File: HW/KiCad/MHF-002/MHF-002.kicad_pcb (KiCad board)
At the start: 2 copper layers, 228 x 101.2 mm, 289 parts, among them J1 VGA, J10 I2C, J100 x, J101 x, J102 x, J103 x, J104 x, J105 x, J106 x, J107 +3V3, J108 GND, J109 +3V3, J11 + 5V -, J110 +5V, J111 GND, J112 GND, J113 SDCard, J12 Reset, J13 +5V, J14 GND, J15 AREF, J16 XTAL2, J17 SDcard, J18 XTAL1, J19 AVCC, J2 PS/2, J20 SDcardpins, J21 x, J22 x, J23 VIN 12V, J24 AND_B1, J25 AND_B2, J26 AND_C1, J27 AND_C2, J28 AND_D1, J29 AND_D2, J3 RCA, J30 AND_Dx, J31 AND_Cx, J32 AND_Bx, J33 NOTF, J34 NOTE, J35 NOTEx, J36 NOTFx, J37 x, J38 x, J39 x, J4 SysBus, J40 x, J41 x, J42 x, J43 x, J44 x, J45 x, J46 x, J47 x, J48 x, J49 x, J5 Micro, J50 x, J51 x, J52 x, J53 x, J54 x, J55 x, J56 x, J57 x, J58 x, J59 x, J6 SysBus, J60 x, J61 x, J62 x, J63 x, J64 x, J65 x, J66 x, J67 x, J68 x, J69 x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

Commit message: footprints (maybe complete)
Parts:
- C1: footprint Capacitor_THT:C_Disc_D4.3mm_W1.9mm_P5.00mm -> MHF:C_Disc_D4.3mm_W1.9mm_P5.00mm
- C10, C11, C13, C14, C15, C16, C2, C5, C6, C7, C8: footprint Capacitor_SMD:C_0603_1608Metric_Pad1.08x0.95mm_HandSolder -> MHF:C_0805_2012Metric_HandSolder
- C12, C9, Cx1, Cx10, Cx11, Cx12, Cx13, Cx2, Cx3, Cx4, Cx5, Cx6, Cx7, Cx8, Cx9: footprint Capacitor_THT:C_Disc_D3.0mm_W2.0mm_P2.50mm -> MHF:C_Disc_D3.0mm_W2.0mm_P2.50mm
- C3, C4: value 100n -> 22n; footprint Capacitor_SMD:C_0603_1608Metric_Pad1.08x0.95mm_HandSolder -> MHF:C_0805_2012Metric_HandSolder
- Cx14, Cx15: footprint Capacitor_THT:CP_Radial_D5.0mm_P2.50mm -> MHF:CP_Radial_D5.0mm_P2.50mm
- D1: footprint Diode_THT:D_DO-41_SOD81_P10.16mm_Horizontal -> MHF:D_DO-41_SOD81_P10.16mm_Horizontal
- D2: footprint Diode_SMD:D_1206_3216Metric -> MHF:D_1210_3225Metric_HandSolder
- D3: footprint Diode_SMD:D_1210_3225Metric -> MHF:D_1210_3225Metric_HandSolder
- F1: footprint Fuse:Fuse_1206_3216Metric_Pad1.42x1.75mm_HandSolder -> MHF:Fuse_1206_3216Metric_Pad1.42x1.75mm_HandSolder
- H5, H6, H7, H8: footprint MountingHole:MountingHole_3.2mm_M3_Pad -> MHF:MountingHole_3.2mm_M3_Pad
- J1: footprint Connector_Dsub:DSUB-15-HD_Socket_Horizontal_P2.29x2.54mm_EdgePinOffset8.35mm_Housed_MountingHolesOffset10.89mm -> MHF:DSUB-15-HD_Socket_Horizontal_P2.29x2.54mm_EdgePinOffset8.35mm_Housed_MountingHolesOffset10.89mm
- J10, J20: footprint Connector_PinHeader_2.54mm:PinHeader_1x04_P2.54mm_Vertical -> MHF:PinHeader_1x04_P2.54mm_Vertical
- J100, J101, J102, J103, J104, J105, J106, J107, J108, J109, J110, J111, J112, J12, J13, J14, J15, J16, J18, J19, J21, J22, J24, J25, J26, J27, J28, J29, J30, J31, J32, J33, J34, J35, J36, J37, J38, J39, J40, J41, J42, J43, J44, J45, J46, J47, J48, J49, J50, J51, J52, J53, J54, J55, J56, J57, J58, J59, J60, J61, J62, J63, J64, J65, J66, J67, J68, J69, J70, J71, J72, J73, J74, J75, J76, J77, J78, J79, J80, J81, J82, J83, J84, J85, J86, J87, J88, J89, J90, J91, J92, J93, J94, J95, J96, J97, J98, J99: footprint Gilhad:PinHole_1x01_2.54xrectangle -> MHF:PinHole_1x01_2.54xrectangle
- J11: footprint Connector_PinSocket_2.54mm:PinSocket_2x03_P2.54mm_Vertical -> MHF:PinSocket_2x03_P2.54mm_Vertical
- J17, J7, J9, JP27, PG1: footprint Connector_PinHeader_2.54mm:PinHeader_1x06_P2.54mm_Vertical -> MHF:PinHeader_1x06_P2.54mm_Vertical
- J23: footprint Connector_BarrelJack:BarrelJack_Horizontal -> MHF:BarrelJack_Horizontal
- J4: footprint Connector_PinSocket_2.54mm:PinSocket_2x32_P2.54mm_Vertical -> MHF:PinSocket_2x32_P2.54mm_Vertical
- J5: footprint Connector_USB:USB_Micro-B_XKB_U254-051T-4BH83-F1S -> MHF:USB_Micro-B_XKB_U254-051T-4BH83-F1S
- J6: footprint Connector_PinHeader_2.54mm:PinHeader_2x32_P2.54mm_Vertical -> MHF:PinHeader_2x32_P2.54mm_Vertical
- J8: footprint Connector_PinHeader_2.54mm:PinHeader_2x03_P2.54mm_Vertical -> MHF:PinHeader_2x03_P2.54mm_Vertical
- JP1, JP10, JP11, JP12, JP13, JP14, JP2, JP3, JP4, JP5, JP6, JP7, JP8, JP9, JP91: footprint Jumper:SolderJumper-2_P1.3mm_Bridged_Pad1.0x1.5mm -> MHF:SolderJumper-2_P1.3mm_Bridged_Pad1.0x1.5mm
- JP100, JP102, JP103, JP104, JP105, JP106, JP107, JP92, JP94, JP95, JP98, JP99: footprint Jumper:SolderJumper-3_P1.3mm_Open_RoundedPad1.0x1.5mm -> MHF:SolderJumper-3_P1.3mm_Open_RoundedPad1.0x1.5mm
- JP15, JP16, JP17, JP18, JP19, JP21, JP22, JP23, JP24, JP25, JP55, JP56: footprint Jumper:SolderJumper-2_P1.3mm_Open_RoundedPad1.0x1.5mm -> MHF:SolderJumper-2_P1.3mm_Open_RoundedPad1.0x1.5mm
- JP26, JP28: footprint Connector_PinHeader_2.54mm:PinHeader_1x02_P2.54mm_Vertical -> MHF:PinHeader_1x02_P2.54mm_Vertical
- LED1, LED10, LED2, LED3, LED4, LED5, LED6, LED7, LED8, LED9: footprint LED_SMD:LED_0805_2012Metric -> MHF:LED_0805_2012Metric
- N1, N3: footprint NetTie:NetTie-2_SMD_Pad0.5mm -> MHF:NetTie-2_SMD_Pad0.5mm
- PA1, PB1, PC1, PD1, PE1, PF1, PH1, PJ1, PK1, PL1: footprint Connector_PinHeader_2.54mm:PinHeader_1x08_P2.54mm_Vertical -> MHF:PinHeader_1x08_P2.54mm_Vertical
- Q1: footprint Package_TO_SOT_THT:TO-92_Inline -> MHF:TO-92_Inline
- R1, R10, R11, R12, R13, R14, R15, R16, R17, R18, R19, R2, R20, R21, R22, R23, R3, R32, R33, R38, R39, R4, R41, R43, R44, R45, R46, R47, R5, R6, R7, R8, R9: footprint Resistor_SMD:R_0805_2012Metric_Pad1.20x1.40mm_HandSolder -> MHF:R_0805_2012Metric_Pad1.20x1.40mm_HandSolder
- R24, R25, R26, R27, R28, R29, R30, R31, R34, R35, R36, R37, R40, R42: footprint Resistor_SMD:R_0603_1608Metric_Pad0.98x0.95mm_HandSolder -> MHF:R_0805_2012Metric_Pad1.20x1.40mm_HandSolder
- U13: footprint Package_SO:SOIC-16_3.9x9.9mm_P1.27mm -> MHF:SOIC-16_3.9x9.9mm_P1.27mm
- U14, U15: footprint Package_TO_SOT_SMD:SOT-223-3_TabPin2 -> MHF:SOT-223-3_TabPin2_HandSolder
- U2, U3: footprint Package_DIP:DIP-14_W7.62mm -> MHF:SOIC-14_3.9x8.7mm_P1.27mm
- U4: footprint Package_SO:TSSOP-20_4.4x5mm_P0.5mm -> MHF:TSSOP-20_4.4x6.5mm_P0.65mm_HandSolder; moved to B.Cu
- U5: footprint MHF:G_SOIC-16_3.9x9.9mm_HandSolder -> MHF:SOIC-16_3.9x9.9mm_P1.27mm
- U7, U8, U9: footprint Package_DIP:DIP-16_W7.62mm -> MHF:SOIC-16_3.9x9.9mm_P1.27mm
- Y1, Y2: footprint Crystal:Crystal_SMD_HC49-SD -> MHF:Crystal_SMD_HC49-SD
- moved C8 220.5 mm to (306.1, 47.8)
- moved C7 220.5 mm to (301.6, 44.9)
- moved C5 220.5 mm to (311.7, 41.4)
- moved C6 220.5 mm to (309.4, 38.7)
- moved U7 189.4 mm to (247.9, -6.94)
- moved J5 175.1 mm to (251.9, -19.9)
- moved Q1 165.7 mm to (252.1, -39.4)
- moved JP20 160.3 mm to (268.5, 136.9)
- moved JP30 160.3 mm to (268.5, 144.5)
- moved JP31 160.3 mm to (268.5, 139.4)
- moved JP32 160.3 mm to (268.5, 141.9)
- moved F1 143.7 mm to (261.1, 35.7)
- moved D3 139.2 mm to (187.1, 141.3)
- moved U15 138.7 mm to (200.9, 156.2)
- moved J17 123.6 mm to (182.9, 82.5)
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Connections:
- M3 pad 13: /L7 -> /L4
- M3 pad 14: /L6 -> /L5
- M3 pad 15: /L5 -> /L6
- M3 pad 16: /L4 -> /L7
- M3 pad 17: /L0 -> /L3
- M3 pad 18: /L1 -> /L2
- M3 pad 19: /L2 -> /L1
- M3 pad 20: /L3 -> /L0
- U4 pad 16: /L0 -> /L3
- U4 pad 17: /L1 -> /L2
- U4 pad 18: /L2 -> /L1
- U4 pad 19: /L3 -> /L0
- U4 pad 2: XAD3 -> XAD7
- U4 pad 3: XAD2 -> XAD6
- U4 pad 4: XAD1 -> XAD5
- U4 pad 5: XAD0 -> XAD4
- U4 pad 6: XAD4 -> XAD3
- U4 pad 7: XAD5 -> XAD2
- U4 pad 8: XAD6 -> XAD1
- U4 pad 9: XAD7 -> XAD0

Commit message: included all planned improvements
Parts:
- added D10: WS2812B, MHF:LED_WS2812B_PLCC4_5.0x5.0mm_P3.2mm_HandSolder, F.Cu at (353.1, 134.6)
- added D11: WS2812B, MHF:LED_WS2812B_PLCC4_5.0x5.0mm_P3.2mm_HandSolder, F.Cu at (363.2, 134.6)
- added D4: WS2812B, MHF:LED_WS2812B_PLCC4_5.0x5.0mm_P3.2mm_HandSolder, F.Cu at (289.6, 134.6)
- added D5: WS2812B, MHF:LED_WS2812B_PLCC4_5.0x5.0mm_P3.2mm_HandSolder, F.Cu at (302.3, 134.6)
- added D6: WS2812B, MHF:LED_WS2812B_PLCC4_5.0x5.0mm_P3.2mm_HandSolder, F.Cu at (312.4, 134.6)
- added D7: WS2812B, MHF:LED_WS2812B_PLCC4_5.0x5.0mm_P3.2mm_HandSolder, F.Cu at (322.6, 134.6)
- added D8: WS2812B, MHF:LED_WS2812B_PLCC4_5.0x5.0mm_P3.2mm_HandSolder, F.Cu at (332.7, 134.6)
- added D9: WS2812B, MHF:LED_WS2812B_PLCC4_5.0x5.0mm_P3.2mm_HandSolder, F.Cu at (342.9, 134.6)
- added J114: VIN, MHF:PinHole_1x01_2.54xrectangle, F.Cu at (325.2, 86.4)
- added J115: VI, MHF:PinHole_1x01_2.54xrectangle, F.Cu at (330.3, 91.4)
- added J116: GND, MHF:PinHole_1x01_2.54xrectangle, F.Cu at (325.2, 94.0)
- added JP29: SBC_D_Dir, MHF:SolderJumper-2_P1.3mm_Open_RoundedPad1.0x1.5mm, F.Cu at (337.9, 66.0)
- added JP33: SBC_A_DIR, MHF:SolderJumper-2_P1.3mm_Open_RoundedPad1.0x1.5mm, F.Cu at (330.3, 68.6)
- added JP34: SBC_G_Enable, MHF:SolderJumper-2_P1.3mm_Open_RoundedPad1.0x1.5mm, F.Cu at (337.9, 73.9)
- added JP35: SBC_S_Enable, MHF:SolderJumper-2_P1.3mm_Open_RoundedPad1.0x1.5mm, F.Cu at (330.3, 76.2)
- added JP36: SBC_Read, MHF:SolderJumper-2_P1.3mm_Open_RoundedPad1.0x1.5mm, F.Cu at (335.4, 81.3)
- added JP37: SBC_Write, MHF:SolderJumper-2_P1.3mm_Open_RoundedPad1.0x1.5mm, F.Cu at (330.3, 83.8)
- added R48: 1k, MHF:R_0805_2012Metric_Pad1.20x1.40mm_HandSolder, F.Cu at (330.3, 96.5)
- added R49: 1k, MHF:R_0805_2012Metric_Pad1.20x1.40mm_HandSolder, F.Cu at (330.3, 99.1)
- J9, PG1: footprint MHF:PinHeader_1x06_P2.54mm_Vertical -> MHF:PinHeader_1x07_P2.54mm_Vertical
- JP92: value X16 -> X_S16
- PA1, PB1, PC1, PD1, PE1, PF1, PH1, PJ1, PK1, PL1: footprint MHF:PinHeader_1x08_P2.54mm_Vertical -> MHF:PinHeader_1x09_P2.54mm_Vertical
- moved LED6 5.68 mm to (45.4, 118.4)
- moved R39 5.68 mm to (48.6, 120.4)
- moved JP20 2.86 mm to (266.7, 134.6)
- moved JP31 2.86 mm to (266.7, 137.2)
- moved JP32 2.86 mm to (266.7, 139.7)
- moved JP30 2.86 mm to (266.7, 142.2)
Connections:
- net Net-(PG1-Pin_6) renamed X_SHARE_FUTURE
- net X16 renamed X_S16
- J9 pad 5: GND -> DTR
- J9 pad 6: +5V -> GND
- JP55 pad 1: SCK -> MISO
- PD1 pad 5: X_SHARE_GRANTED -> Net-(PD1-Pin_5)
- PD1 pad 6: X_SHARE_REQUEST -> Net-(PD1-Pin_6)
- PG1 pad 5: Net-(PG1-Pin_5) -> X_SHARE_REQUEST
- U1 pad 29: Net-(PG1-Pin_5) -> X_SHARE_REQUEST
- U1 pad 47: X_SHARE_GRANTED -> Net-(PD1-Pin_5)
- U1 pad 48: X_SHARE_REQUEST -> Net-(PD1-Pin_6)

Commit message: MHF-002 routing full PCB, need add texts
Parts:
- removed D10, D11: WS2812B, MHF:LED_WS2812B_PLCC4_5.0x5.0mm_P3.2mm_HandSolder
- removed J20: SDcardpins, MHF:PinHeader_1x04_P2.54mm_Vertical
- C12: value 100n -> 100n RESET; moved to F.Cu
- C3, C4, JP21, JP22, JP23, JP24, JP25, N1, N3, R14, R15, R2, R24, R27, R3, R36, R39, R47, R48, R49, R5, U2, U3, U5, U9, Y2: moved to B.Cu
- C9: value 100n -> DTR 100n; moved to F.Cu
- D1: footprint MHF:D_DO-41_SOD81_P10.16mm_Horizontal -> MHF:D_DO-41_SOD81_P9.4mm_Horizontal
- J24, J25, J26, J27, J28, J29, J30, J31, J32, JP10, JP11, JP5, JP6, JP7, JP8, JP9, R16, R17, R18, R19, R20, R21, R22, R23, R30, R31, R32, R33: moved to F.Cu
- LED1: value RX -> RX0
- LED2: value TX -> TX0
- LED4: value CTS -> CTS0
- LED5: value RTS -> RTS0
- R37: value 10k -> 1k
- R40: value 1k -> HALTdown 1k
- R42: value 1k -> HALTup 1k
- R46: value 10k -> 1k; moved to B.Cu
- moved JP21 272.5 mm to (214.1, 105.3)
- moved JP23 268.7 mm to (210.5, 110.9)
- moved JP22 268.0 mm to (210.3, 105.5)
- moved JP25 267.7 mm to (210.5, 113.9)
- moved JP24 267.2 mm to (210.5, 108.4)
- moved JP17 259.8 mm to (241.3, 31.8), turned to 90 degrees
- moved JP19 257.7 mm to (238.8, 31.8), turned to 90 degrees
- moved JP18 254.9 mm to (236.2, 31.8), turned to 90 degrees
- moved JP15 252.0 mm to (233.7, 31.8), turned to 90 degrees
- moved JP16 249.5 mm to (231.1, 31.8), turned to 90 degrees
- moved JP27 241.1 mm to (223.5, 96.5), turned to 180 degrees
- moved JP28 235.4 mm to (240.0, 55.9)
- moved JP26 231.8 mm to (231.1, 58.4), turned to 90 degrees
- moved LED9 229.9 mm to (249.9, 64.5)
- moved R46 225.8 mm to (249.9, 64.5), turned to 180 degrees
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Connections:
- J9 pad 1: RTS -> RTS0
- J9 pad 2: CTS -> CTS0
- J9 pad 3: RX -> DTR
- J9 pad 4: TX -> RX0
- J9 pad 5: DTR -> TX0
- JP15 pad 2: M8TXD -> RX0
- JP16 pad 2: M8RXD -> TX0
- JP17 pad 2: CTS -> RTS0
- JP19 pad 2: RTS -> CTS0
- JP21 pad 2: M8TXD -> RX0
- JP22 pad 2: M8RXD -> TX0
- JP23 pad 2: CTS -> RTS0
- JP25 pad 2: RTS -> CTS0
- LED1 pad 1: M8RXD -> RX0
- LED2 pad 1: M8TXD -> TX0
- PB1 pad 5: CTS -> CTS0
- PB1 pad 6: RTS -> RTS0
- PE1 pad 1: TX -> RX0
- PE1 pad 2: RX -> TX0
- R30 pad 1: RX -> Net-(JP15-A)
- R30 pad 2: M8RXD -> Net-(U13-TXD)
- R31 pad 1: TX -> Net-(JP16-A)
- R31 pad 2: M8TXD -> Net-(U13-RXD)
- R37 pad 2: CTS -> CTS0
- R38 pad 2: RTS -> RTS0
- U1 pad 2: TX -> RX0
- U1 pad 23: CTS -> CTS0
- U1 pad 24: RTS -> RTS0
- U1 pad 3: RX -> TX0
- U13 pad 2: Net-(JP15-A) -> Net-(U13-TXD)
- U13 pad 3: Net-(JP16-A) -> Net-(U13-RXD)
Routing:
- net X_SHARE_DIRTY: track 0.00 -> 159.9 mm, vias 0 -> 4
- net RTS0: track 0.00 -> 158.4 mm, vias 0 -> 2
- net Shared_data_D0: track 0.00 -> 154.7 mm, vias 0 -> 2
- net X_S16: track 0.00 -> 154.1 mm, vias 0 -> 7
- net RX0: track 0.00 -> 152.4 mm, vias 0 -> 3
- net TX0: track 0.00 -> 151.8 mm, vias 0 -> 3
- net CTS0: track 0.00 -> 150.0 mm, vias 0 -> 3
- net X_READ: track 0.00 -> 146.3 mm, vias 0 -> 4
- net Shared_data_D2: track 0.00 -> 141.2 mm, vias 0 -> 4
- net Bb: track 0.00 -> 133.7 mm, vias 0 -> 2
- net SIGNAL_RCA: track 0.00 -> 127.1 mm, vias 0 -> 6
- net Net-(PD1-Pin_5): track 0.00 -> 126.5 mm, vias 0 -> 5
- net SCL: track 0.00 -> 126.5 mm, vias 0 -> 3
- net SDA: track 0.00 -> 125.4 mm, vias 0 -> 1
- net SS: track 0.00 -> 124.0 mm, vias 0 -> 2
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- added copper zone on In2.Cu, net +5V
- added copper zone on In1.Cu, net GND
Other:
- board size 228 x 101.2 mm -> 100 x 100 mm
- copper layers 2 -> 4
- board text added: "CH340"
- board text added: "I2Cup"

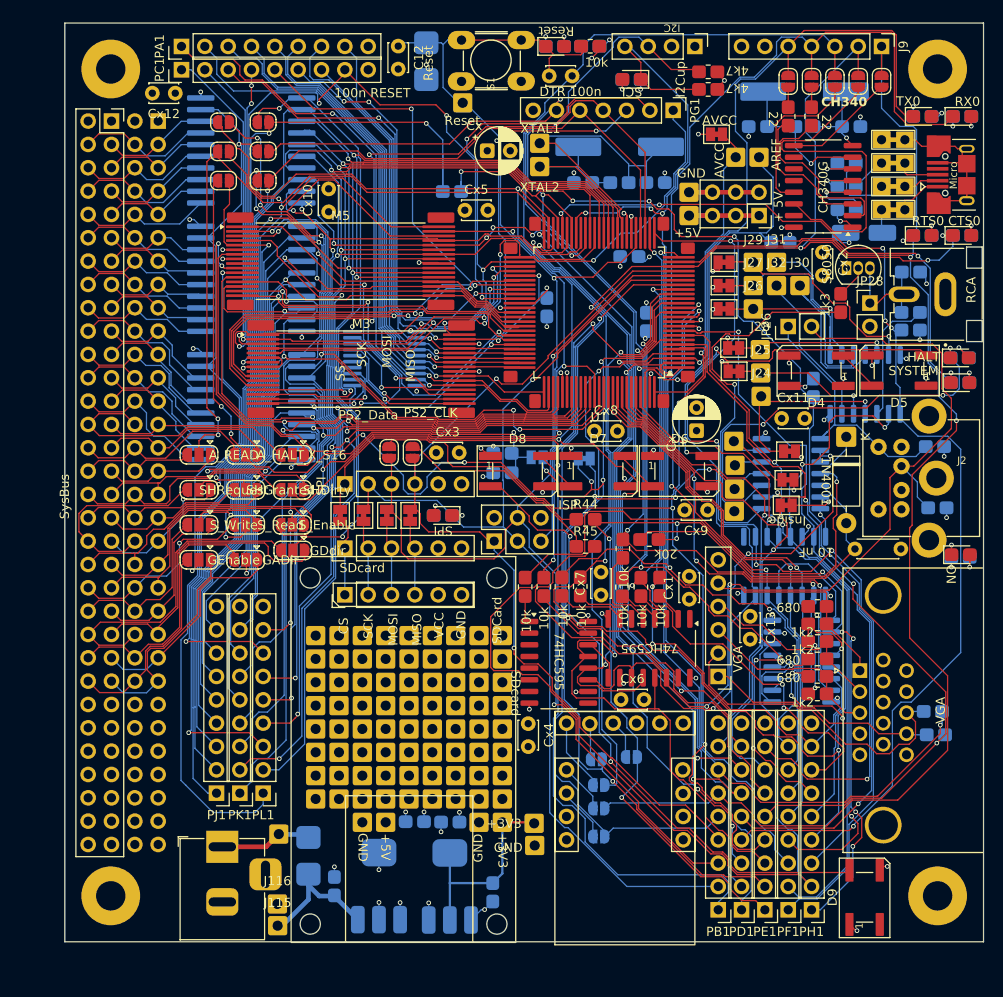
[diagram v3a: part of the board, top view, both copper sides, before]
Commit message: improved SystemBus and 3xAND, NOT
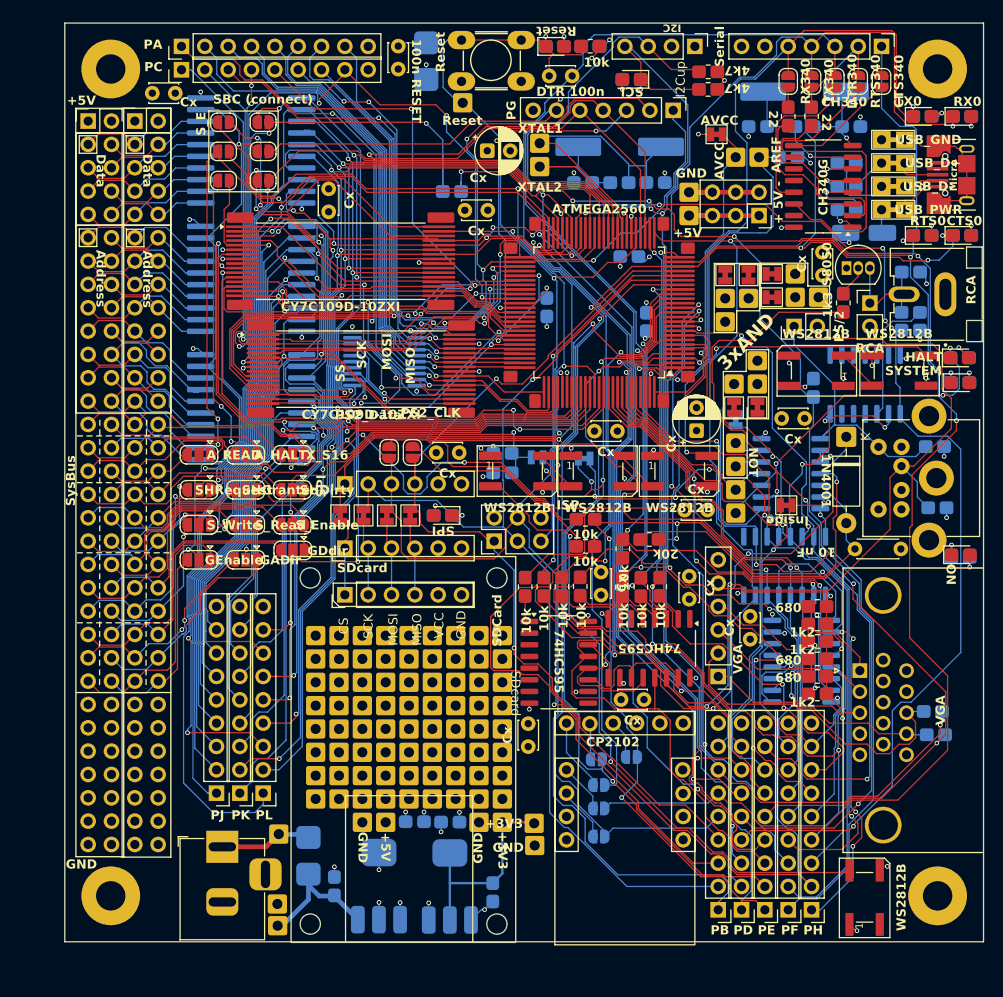
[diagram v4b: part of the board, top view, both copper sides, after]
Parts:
- J6: footprint MHF:PinHeader_2x32_P2.54mm_Vertical -> MHF:PinHeader_2x32_P2.54mm_Vertical_down; moved to F.Cu
- JP11: moved to B.Cu
- JP13: value Xhalt -> XHalt
- PA1: value PA0 -> PA
- PB1: value PB0 -> PB
- PC1: value PC0 -> PC
- PD1: value PD0 -> PD
- PE1: value PE0 -> PE
- PF1: value PF0 -> PF
- PG1: value PG0 -> PG
- PH1: value PH0 -> PH
- PJ1: value PJ0 -> PJ
- PK1: value PK0 -> PK
- PL1: value PL0 -> PL
- moved C5 9.29 mm to (231.2, 40.0)
- moved JP11 8.67 mm to (225.4, 68.6), turned to -90 degrees
- moved J31 8.55 mm to (224.3, 57.9), turned to -90 degrees
- moved J32 8.44 mm to (227.8, 62.2), turned to 90 degrees
- moved JP9 6.92 mm to (229.4, 55.2)
- moved J28 6.86 mm to (231.9, 55.2)
- moved JP5 5.92 mm to (227.8, 67.2), turned to 90 degrees
- moved JP10 5.36 mm to (229.4, 52.7)
- moved J29 4.75 mm to (231.9, 52.7)
- moved JP6 3.93 mm to (225.2, 67.2), turned to 90 degrees
- moved JP7 3.69 mm to (224.3, 52.8), turned to -90 degrees
- moved J26 3.26 mm to (224.3, 55.4), turned to -90 degrees
- moved J25 3.14 mm to (225.2, 64.7), turned to 90 degrees
- moved JP8 2.90 mm to (226.8, 52.8), turned to -90 degrees
- moved J4 2.54 mm to (154.9, 36.1)
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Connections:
- D9 pad 2: Net-(D10-DIN) -> unconnected-(D9-DOUT-Pad2)
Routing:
- net Net-(J27-Pin_1): track 23.8 -> 0.00 mm
- net Net-(J29-Pin_1): track 23.7 -> 0.06 mm, vias 1 -> 0
- net Net-(J24-Pin_1): track 21.0 -> 0.00 mm, vias 1 -> 0
- net Net-(J31-Pin_1): track 17.4 -> 0.00 mm
- net Net-(J30-Pin_1): track 17.0 -> 0.00 mm
- net Net-(J32-Pin_1): track 16.8 -> 0.00 mm
- net Net-(J28-Pin_1): track 16.7 -> 0.00 mm, vias 1 -> 0
- net Net-(J25-Pin_1): track 16.4 -> 0.00 mm, vias 1 -> 0
- net Net-(J26-Pin_1): track 16.2 -> 0.00 mm, vias 1 -> 0
- net +5V: track 102.3 -> 92.0 mm, vias 56 -> 49
- net Net-(J35-Pin_1): track 46.3 -> 37.2 mm
- net B_SHARE_REQUEST: track 22.5 -> 13.9 mm, vias 0 -> 1
- net B_S_ENABLE: track 35.1 -> 26.8 mm
- net B16: track 29.1 -> 20.9 mm
- net B_G_D_DIR: track 35.1 -> 28.0 mm
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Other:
- board text added: "3xAND"
- board text added: "Address"
- board text added: "Data"
- board text added: "SBC (connect)"
- board text added: "S_E"
